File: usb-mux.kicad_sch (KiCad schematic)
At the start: 4 parts, among them U16 FSUSB42MUX

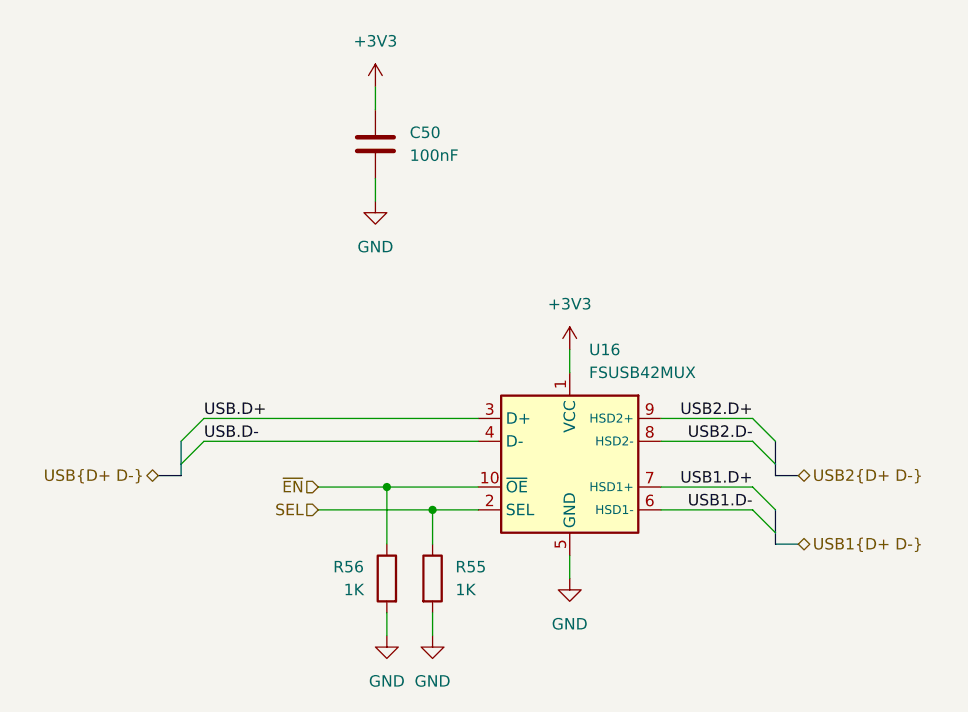
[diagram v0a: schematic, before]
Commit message: Address board review comments
- Add pull-ups for both I2C busses (4K7)
- Set eFuse limit to 600mA (400mA before)
- Label StemmaQt as such in schematics
- Fix typo in USB Port value
- Fix USB Mux to be disabled by default (pull-down to pull-up)
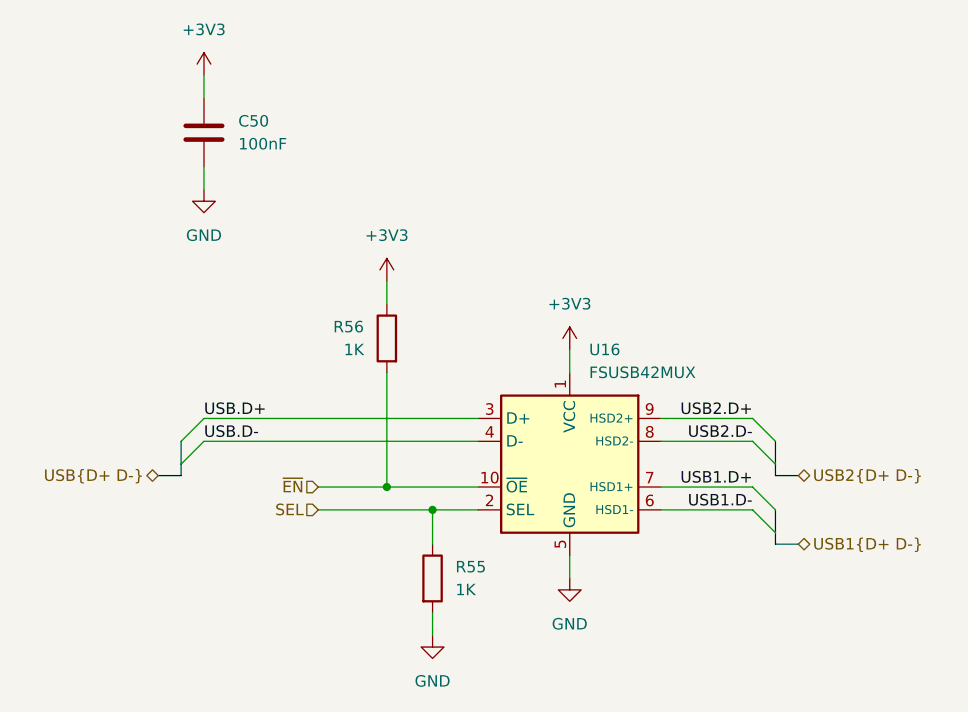
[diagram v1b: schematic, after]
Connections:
- net +3V3: now also R56.1
- net GND: no longer R56.2
- net ~{EN}: now also R56.2; no longer R56.1
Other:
- moved on the sheet: C50, R56
